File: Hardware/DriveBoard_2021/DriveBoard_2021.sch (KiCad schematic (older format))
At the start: 10 parts, among them U1 TM4C129E_Launchpad

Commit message: Added Molex connectors, added all serial connections, added LED indicators
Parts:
- added BL_WHL (x2), FL_WHL, FR_WHL: Molex_SL_03, symbol MRDT_Connectors:Molex_SL_03
- added C10, C7: 1uF, symbol Device:C_Small
- added C11, C8: 0.1uF, symbol Device:C_Small
- added C12, C9: 0.33uF, symbol Device:C_Small
- added R1, R2, R3, R4, R5, R6, R7, R8, R9: 500, symbol Device:R
- added U1, U2: MAX_3232, symbol MRDT_ICs:MAX_3232
- added blue (x8), green: LED, symbol Device:LED
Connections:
- net labels added: BL_IN, BL_OUT, BR_IN, BR_OUT, FL_IN, FL_OUT, FR_IN, FR_OUT, Rx2, Rx3, Rx4, Rx6, Tx2, Tx3, Tx4, Tx6
- wire segments 38 -> 127
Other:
- note added: "BK_WHLS"
- note added: "FR_WHLS"

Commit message: Adjusted PWR, Added Switches, Added LED indicators
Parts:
- removed C1, C2, C3, C4: 10uF, symbol Device:C
- removed U?: 5V OKI, symbol MRDT_Devices:OKI
- removed U?: 3V3 OKI, symbol MRDT_Devices:OKI
- added C1: 100uF, symbol Device:C_Small
- added C2: 1000uF, symbol Device:C_Small
- added D1: 1N5822, Diode_THT:D_DO-201AD_P15.24mm_Horizontal, symbol Diode:1N5822
- added L1: 100uH, symbol Device:L
- added LED1, LED2: green, symbol Device:LED
- added LED12, LED13, LED14, LED15, LED16, LED17: RED, symbol Device:LED
- added R10, R11, R12, R13, R14, R15, R16, R17: 500, symbol Device:R
- added SW1, SW2, SW3, SW4, SW5, SW6: SW_Push, symbol Switch:SW_Push
- added U1: LM2576S-3.3, Package_TO_SOT_SMD:TO-263-5_TabPin3, symbol Regulator_Switching:LM2576S-3.3
- LED10, LED11, LED4, LED5, LED6, LED7, LED8, LED9: renamed from blue; value LED -> blue
- LED3: renamed from green; value LED -> green
- renumbered C12 to C10, C5 to C3, C6 to C4, C7 to C5, C8 to C6, C9 to C7, C10 to C8, C11 to C9
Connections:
- net labels added: BL_DRIVE, BR_DRIVE, FL_DRIVE, FR_DRIVE, LT_TURN, RT_TURN
- net labels removed: +5V
- wire segments 127 -> 195
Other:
- note added: "POWER\n"
- note added: "SWITCHES"
- moved on the sheet: BL_WHL, C10, C3, C4, C5, C6, C7, C8, C9, Conn1A, Conn1B, Conn1C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

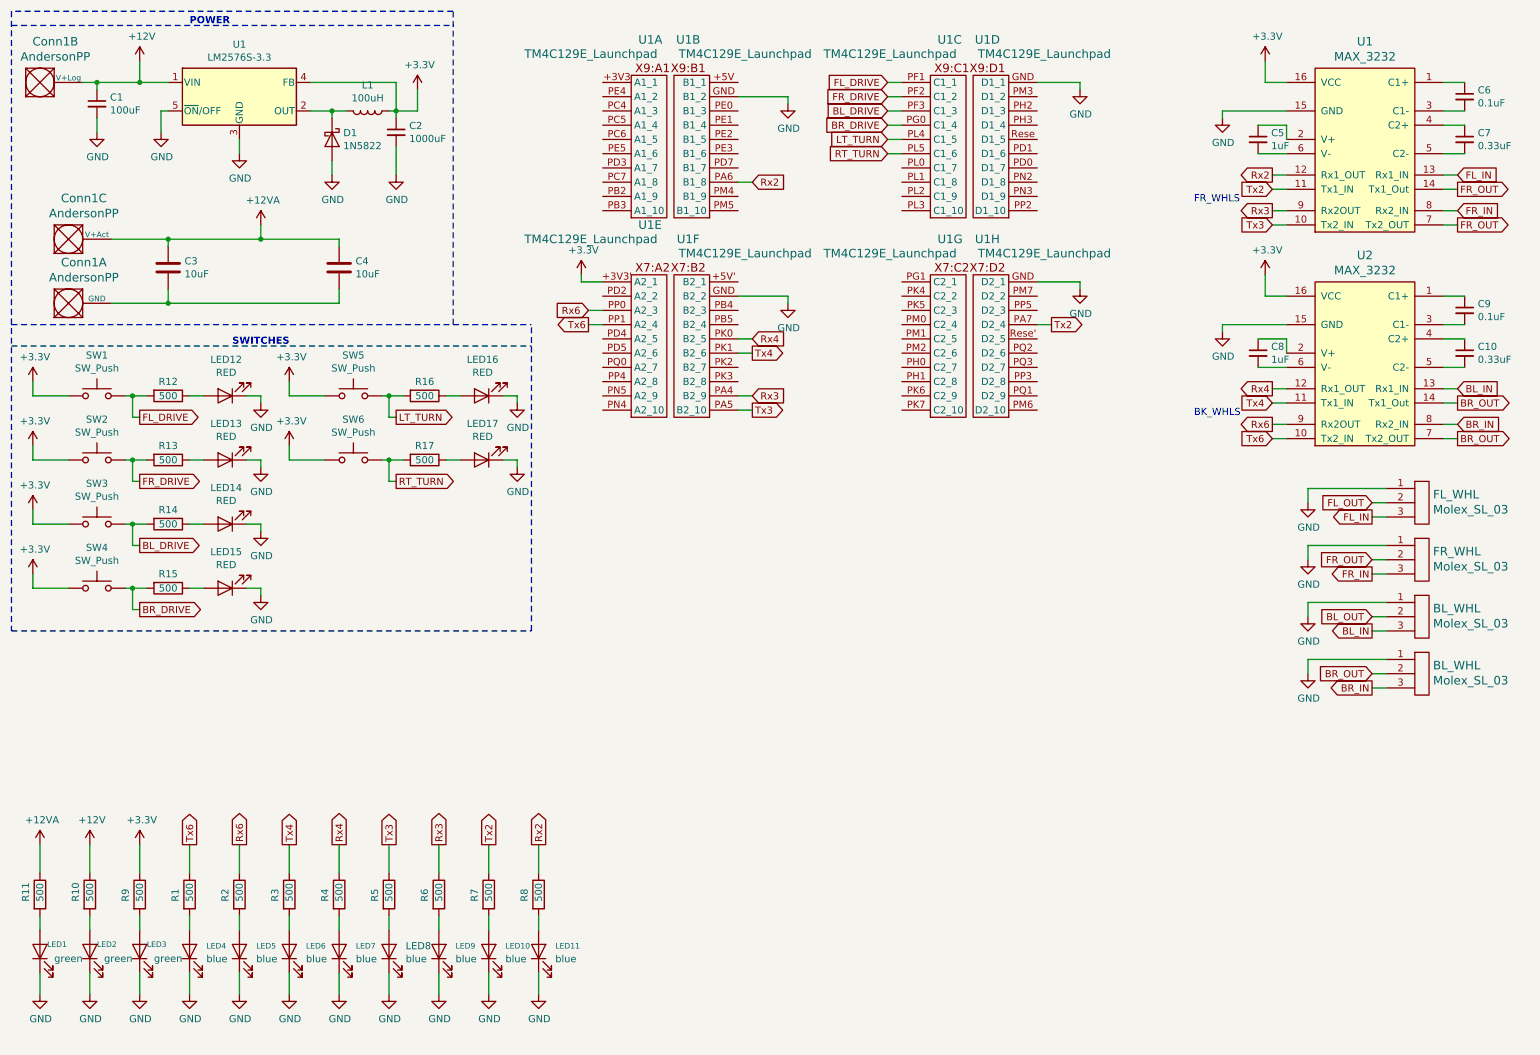
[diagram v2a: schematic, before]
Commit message: ODrive PWR terminal added
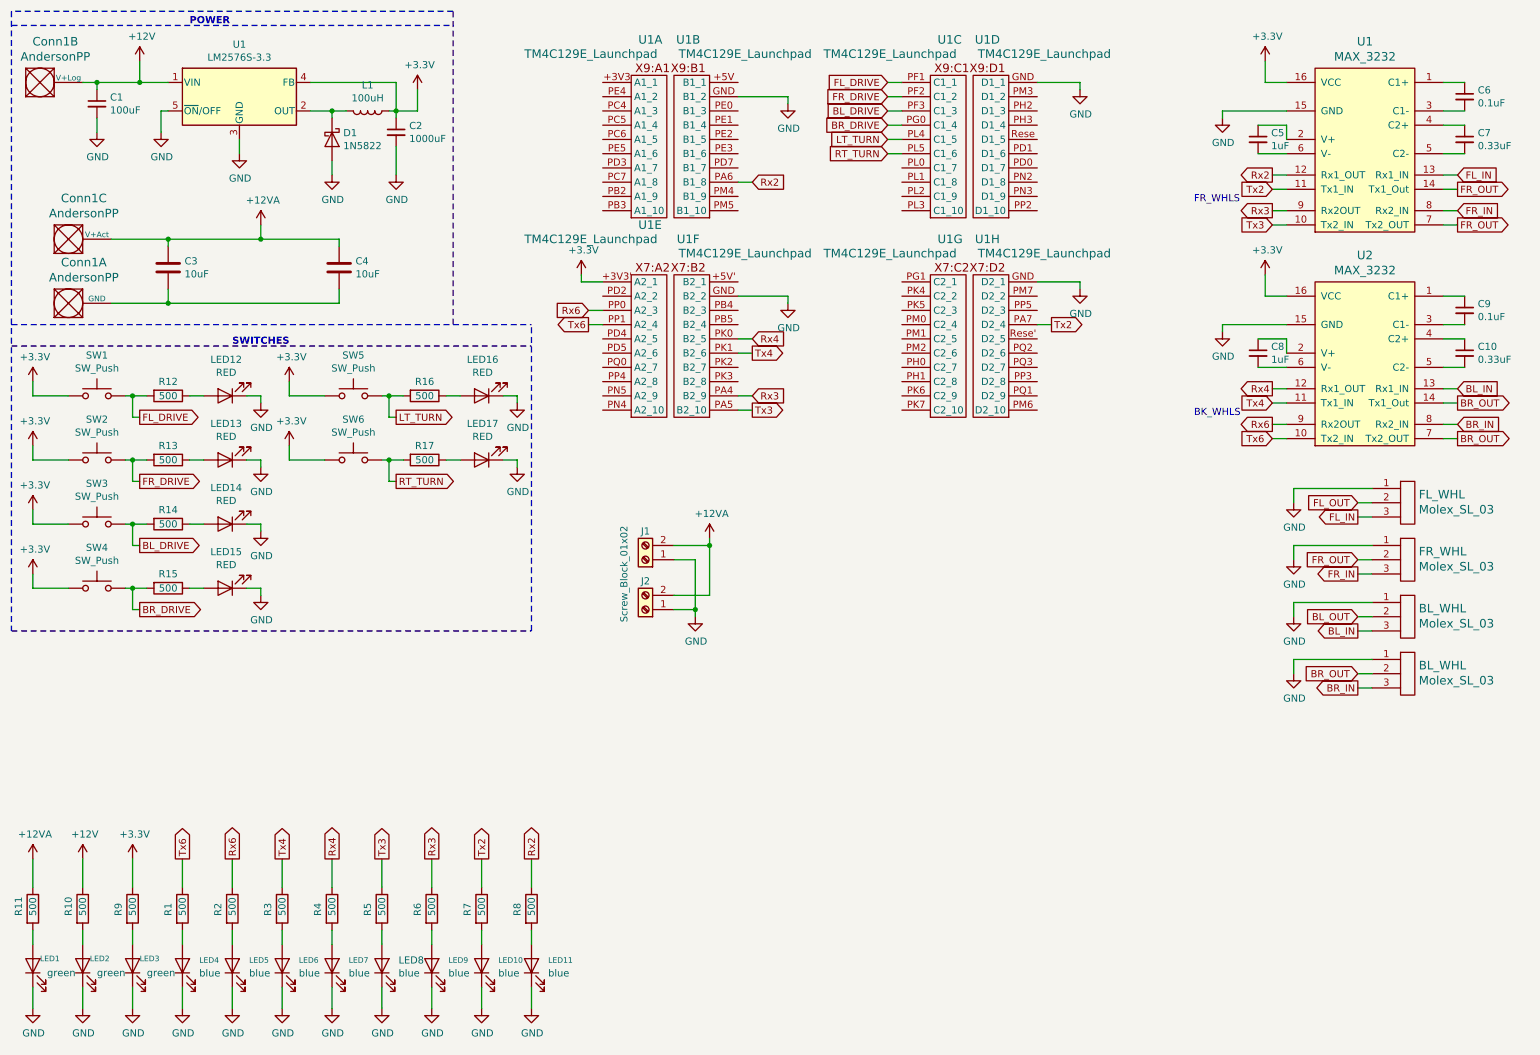
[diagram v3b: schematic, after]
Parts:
- added J1: Screw_Block_01x02, symbol Connector:Screw_Terminal_01x02
- added J2: Screw_Terminal_01x02, symbol Connector:Screw_Terminal_01x02
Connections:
- net +12VA: now also J1.2 (Pin_2), J2.2 (Pin_2)
- net GND: now also J1.1 (Pin_1), J2.1 (Pin_1)
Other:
- moved on the sheet: BL_WHL, FL_WHL, FR_WHL, LED1, LED10, LED11, LED2, LED3, LED4, LED5, LED6, LED7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

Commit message: Added CAN Controller and Transceiver
Need to verify 16Mhz is correct oscillator for use. Must be parallel cut crystall.
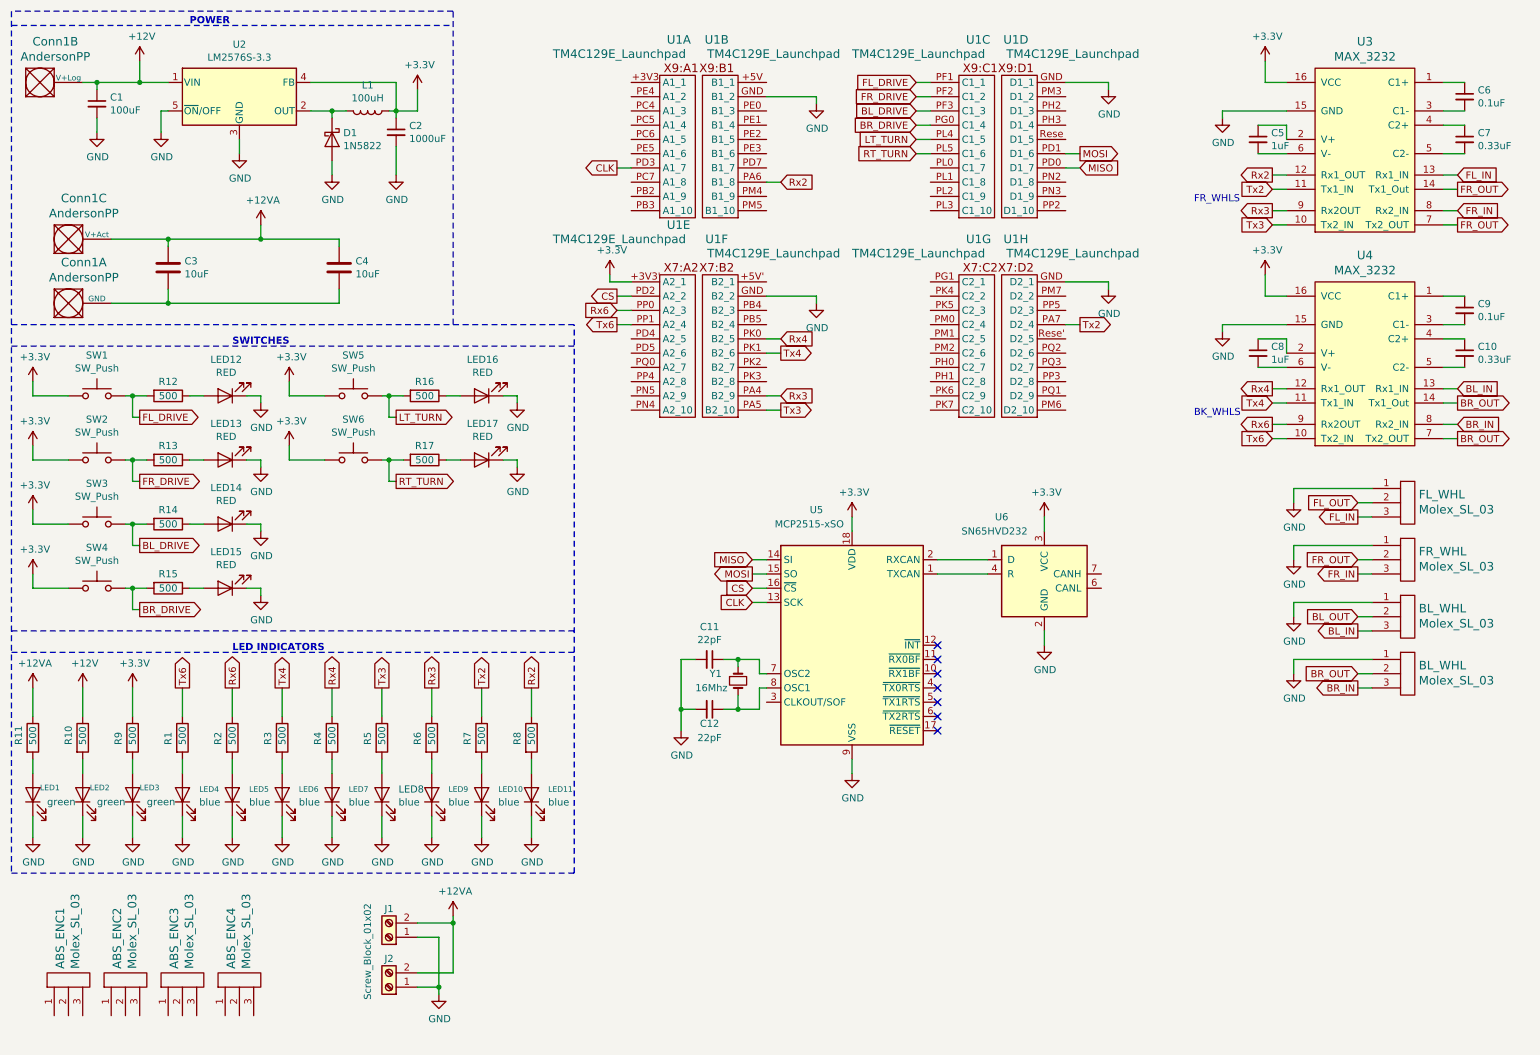
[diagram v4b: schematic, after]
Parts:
- added ABS_ENC1, ABS_ENC2, ABS_ENC3, ABS_ENC4: Molex_SL_03, symbol MRDT_Connectors:Molex_SL_03
- added C11, C12: 22pF, symbol Device:C_Small
- added U5: MCP2515-xSO, Package_SO:SOIC-18W_7.5x11.6mm_P1.27mm, symbol Interface_CAN_LIN:MCP2515-xSO
- added U6: SN65HVD232, Package_SO:SOIC-8_3.9x4.9mm_P1.27mm, symbol Interface_CAN_LIN:SN65HVD232
- added Y1: 16Mhz, symbol Device:Crystal_Small
- renumbered U1 to U2, U1 to U3, U2 to U4
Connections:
- net +3V3: now also U5.18 (VDD), U6.3 (VCC)
- net GND: now also C11.2, C12.2, U5.9 (VSS), U6.2 (GND)
- net CLK: now reaches U1.PD3 (A1_7)
- net CLK: now also U5.13 (SCK)
- net MISO: now reaches U1.PD0 (D1_7)
- net MISO: now also U5.14 (SI)
- net MOSI: now reaches U1.PD1 (D1_6)
- net MOSI: now also U5.15 (SO)
- net CS: now reaches U1.PD2 (A2_2)
- net CS: now also U5.16 (~CS)
- new net: U5.1 (TXCAN), U6.4 (R)
- new net: U5.2 (RXCAN), U6.1 (D)
- new net: C11.1, U5.7 (OSC2), Y1.1
- new net: C12.1, U5.8 (OSC1), Y1.2
- no-connect marks 0 -> 7
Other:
- note added: "LED INDICATORS"
- moved on the sheet: J1, J2, LED1, LED10, LED11, LED2, LED3, LED4, LED5, LED6, LED7, LED8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

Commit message: Fixing CAN Hookup with Transceiver
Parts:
- removed J1: Screw_Block_01x02, symbol Connector:Screw_Terminal_01x02
- removed J2: Screw_Terminal_01x02, symbol Connector:Screw_Terminal_01x02
- added Conn? (x2): AndersonPP, symbol MRDT_Connectors:AndersonPP
- added U?: MCP2551-I-SN, Package_SO:SOIC-8_3.9x4.9mm_P1.27mm, symbol Interface_CAN_LIN:MCP2551-I-SN
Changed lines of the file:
@@
-$EndComp
-$Comp
-L Connector:Screw_Terminal_01x02 J1
-U 1 1 5F831E4A
-P 3150 7000
-F 0 "J1" H 3150 6800 50  0000 C CNN
-F 1 "Screw_Block_01x02" V 3300 7100 50  0000 C CNN
-F 2 "" H 3150 7000 50  0001 C CNN
-F 3 "~" H 3150 7000 50  0001 C CNN
-	1    3150 7000
-	-1   0    0    1
-$EndComp
-$Comp
-L Connector:Screw_Terminal_01x02 J2
-U 1 1 5F83F102
-P 3150 7350
-F 0 "J2" H 3150 7150 50  0000 C CNN
-F 1 "Screw_Terminal_01x02" H 2050 7050 50  0001 C CNN
-F 2 "" H 3150 7350 50  0001 C CNN
-F 3 "~" H 3150 7350 50  0001 C CNN
-	1    3150 7350
-	-1   0    0    1
 $EndComp
 $Comp
@@
 NoConn ~ 7000 5450
 NoConn ~ 7000 5550
+$Comp
+L Interface_CAN_LIN:MCP2551-I-SN U?
+U 1 1 5FABA995
+P 8300 5700
+F 0 "U?" H 8300 6281 50  0000 C CNN
+F 1 "MCP2551-I-SN" H 8300 6190 50  0000 C CNN
+F 2 "Package_SO:SOIC-8_3.9x4.9mm_P1.27mm" H 8300 5200 50  0001 C CIN
+F 3 "http://ww1.microchip.com/downloads/en/devicedoc/21667d.pdf" H 8300 5700 50  0001 C CNN
+	1    8300 5700
+	1    0    0    -1
+$EndComp
+$Comp
+L MRDT_Connectors:AndersonPP Conn?
+U 3 1 5FACBAC8
+P 2650 7050
+F 0 "Conn?" H 2858 7437 60  0000 C CNN
+F 1 "AndersonPP" H 2858 7331 60  0000 C CNN
+F 2 "" H 2500 6500 60  0001 C CNN
+F 3 "" H 2500 6500 60  0001 C CNN
+	3    2650 7050
+	1    0    0    -1
+$EndComp
+$Comp
+L MRDT_Connectors:AndersonPP Conn?
+U 1 1 5FACBACE
+P 2650 7500
+F 0 "Conn?" H 2858 7887 60  0000 C CNN
+F 1 "AndersonPP" H 2858 7781 60  0000 C CNN
+F 2 "" H 2500 6950 60  0001 C CNN
+F 3 "" H 2500 6950 60  0001 C CNN
+	1    2650 7500
+	1    0    0    -1
+$EndComp
 $EndSCHEMATC

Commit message: Fixed CAN Transceiver. Added Anderson PWR connections for ODrives
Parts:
- removed C10, C7: 0.33uF, symbol Device:C_Small
- removed C11, C12: 22pF, symbol Device:C_Small
- removed C5, C8: 1uF, symbol Device:C_Small
- removed C6, C9: 0.1uF, symbol Device:C_Small
- removed Conn? (x2): AndersonPP, symbol MRDT_Connectors:AndersonPP
- removed U3, U4: MAX_3232, symbol MRDT_ICs:MAX_3232
- removed U5: MCP2515-xSO, Package_SO:SOIC-18W_7.5x11.6mm_P1.27mm, symbol Interface_CAN_LIN:MCP2515-xSO
- removed U6: SN65HVD232, Package_SO:SOIC-8_3.9x4.9mm_P1.27mm, symbol Interface_CAN_LIN:SN65HVD232
- removed Y1: 16Mhz, symbol Device:Crystal_Small
- added C3: 100uF, symbol Device:C_Small
- added C4: 1000uF, symbol Device:C_Small
- added Conn2, Conn3: AndersonPP, symbol MRDT_Connectors:AndersonPP
- added D2: 1N5822, Diode_THT:D_DO-201AD_P15.24mm_Horizontal, symbol Diode:1N5822
- added L2: 100uH, symbol Device:L
- added R18: 120, symbol Device:R_Small
- added U3: LM2576HVS-5, Package_TO_SOT_SMD:TO-263-5_TabPin3, symbol Regulator_Switching:LM2576HVS-5
- U1: symbol MRDT_Shields:TM4C129E_Launchpad -> DriveBoard_2021-rescue:TM4C129E_Launchpad-MRDT_Shields
- gave numbers to parts that had none: 1
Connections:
- net +12V: now also C3.1, U3.1 (VIN)
- net +12VA: now also Conn2.3 (V+Act), Conn3.3 (V+Act)
- net BL_IN: now also U1.PK0 (B2_5)
- net BL_OUT: now also U1.PK1 (B2_6)
- net BR_IN: now also U1.PP0 (A2_3)
- net BR_OUT: now also U1.PP1 (A2_4)
- net FL_IN: now also U1.PA6 (B1_8)
- net FL_OUT: now also U1.PA7 (D2_4)
- net FR_IN: now also U1.PA4 (B2_9)
- net FR_OUT: now also U1.PA5 (B2_10)
- net GND: now also U4.2 (VSS), C3.2, C4.2, Conn2.1 (GND), Conn3.1 (GND), D2.2 (A), U3.3 (GND), U3.5 (~ON~/OFF)
- net Rx2: no longer U1.PA6 (B1_8)
- net Rx3: no longer U1.PA4 (B2_9)
- net Rx4: no longer U1.PK0 (B2_5)
- net Rx6: no longer U1.PP0 (A2_3)
- net Tx2: no longer U1.PA7 (D2_4)
- net Tx3: no longer U1.PA5 (B2_10)
- net Tx4: no longer U1.PK1 (B2_6)
- net Tx6: no longer U1.PP1 (A2_4)
- net CAN_Rx: now reaches U1.PD4 (A2_5)
- net CAN_Rx: now also U4.1 (TXD)
- net CAN_Tx: now reaches U1.PD5 (A2_6)
- net CAN_Tx: now also U4.4 (RXD)
- net +5V: now reaches U4.3 (VDD)
- net +5V: now also C4.1, L2.1, U3.4 (FB)
- net CANL: now reaches U4.6 (CANL)
- net CANL: now also R18.2
- net CANH: now reaches U4.7 (CANH)
- net CANH: now also R18.1
- net CLK: no longer names the net of U1.PD3 (A1_7)
- net CS: no longer names the net of U1.PD2 (A2_2)
- net MISO: no longer names the net of U1.PD0 (D1_7)
- net MOSI: no longer names the net of U1.PD1 (D1_6)
- new net: D2.1 (K), L2.2, U3.2 (OUT)
- no-connect marks 7 -> 2
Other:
- note added: "Motor Molex Connections"
- note added: "ODrive PWR Connections"
- note added: "Serial 0"
- note added: "Serial 2 Rx"
- note added: "Serial 2\nTx\n"
- note added: "Serial 3"
- note added: "Serial 4"
- note added: "Serial 6"
- note added: "TIVA"
- note removed: "BK_WHLS"
- note removed: "FR_WHLS"
- moved on the sheet: ABS_ENC1, ABS_ENC2, ABS_ENC3, ABS_ENC4, BL_WHL, C3, C4, Conn1A, Conn1C, FL_WHL, FR_WHL, LED1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
